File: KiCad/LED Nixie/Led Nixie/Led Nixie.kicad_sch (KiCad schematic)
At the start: 26 parts, among them J1 Conn_01x06_Socket, J2 Conn_01x06_Socket, J3 Conn_01x06_Pin, J4 Conn_01x06_Pin, U1 74HC595, U2 74HC595

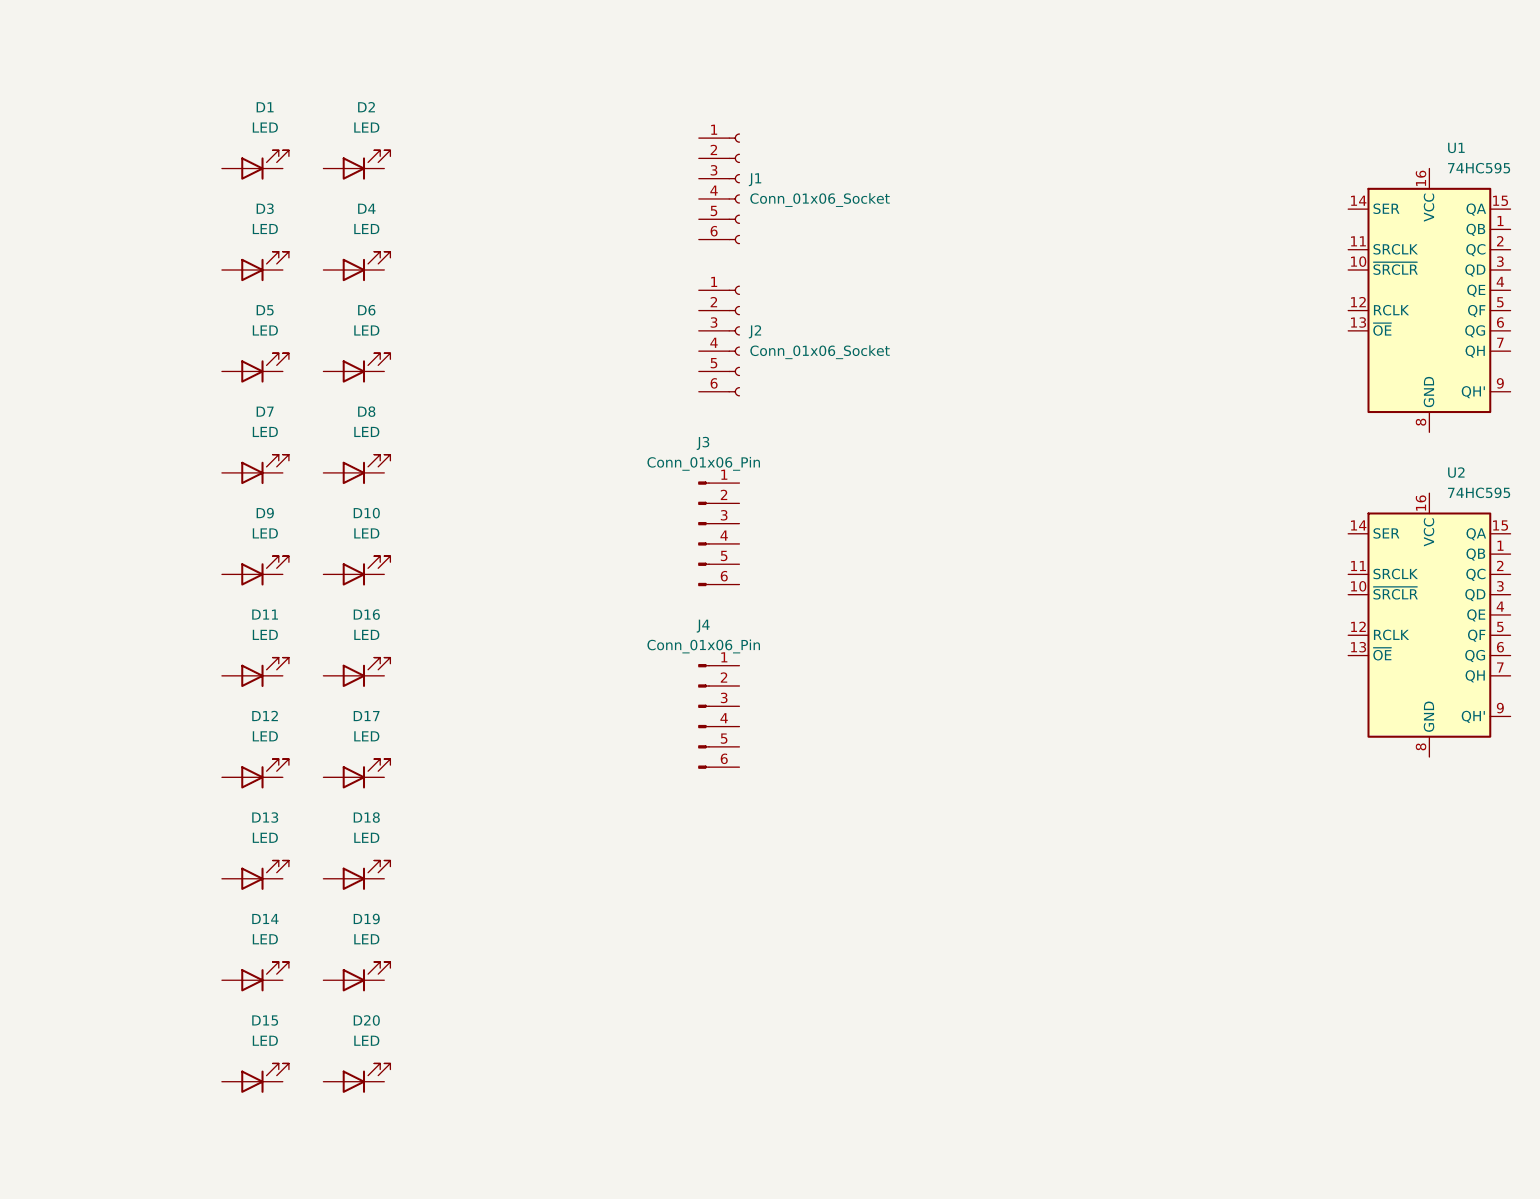
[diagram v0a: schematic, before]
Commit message: Updated Nixie-PCB
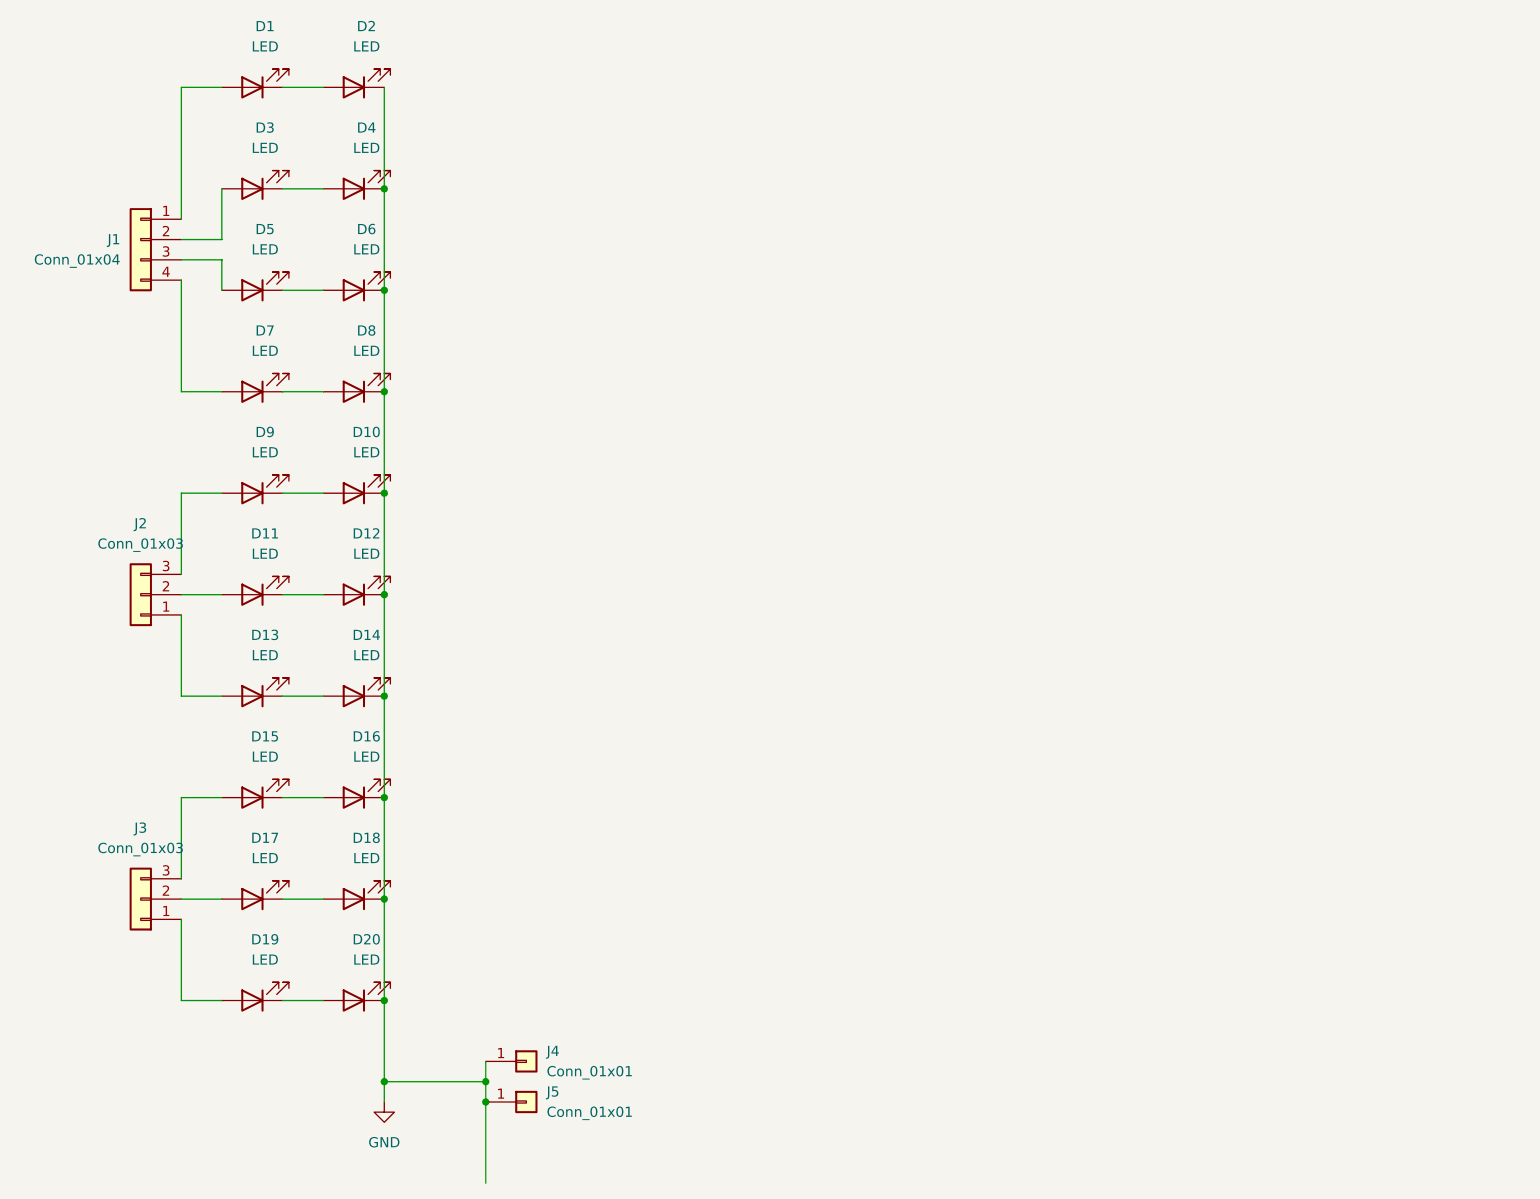
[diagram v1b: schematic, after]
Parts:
- removed J1, J2: Conn_01x06_Socket, symbol Connector:Conn_01x06_Socket
- removed J3, J4: Conn_01x06_Pin, symbol Connector:Conn_01x06_Pin
- removed U1, U2: 74HC595, symbol 74xx:74HC595
- added J1: Conn_01x04, Connector_PinHeader_2.00mm:PinHeader_1x04_P2.00mm_Vertical, symbol Connector_Generic:Conn_01x04
- added J2, J3: Conn_01x03, Connector_PinHeader_2.00mm:PinHeader_1x03_P2.00mm_Vertical, symbol Connector_Generic:Conn_01x03
- added J4, J5: Conn_01x01, Connector_PinHeader_2.00mm:PinHeader_1x01_P2.00mm_Vertical, symbol Connector_Generic:Conn_01x01
- D1, D10, D11, D2, D20, D3, D4, D5, D6, D7, D8, D9: footprint LED_SMD:LED_1206_3216Metric -> custom_footprints:LED_1206_3216Metric_nosilkscreen
- D12: renamed from D16; footprint LED_SMD:LED_1206_3216Metric -> custom_footprints:LED_1206_3216Metric_nosilkscreen
- D13: renamed from D12; footprint LED_SMD:LED_1206_3216Metric -> custom_footprints:LED_1206_3216Metric_nosilkscreen
- D14: renamed from D17; footprint LED_SMD:LED_1206_3216Metric -> custom_footprints:LED_1206_3216Metric_nosilkscreen
- D15: renamed from D13; footprint LED_SMD:LED_1206_3216Metric -> custom_footprints:LED_1206_3216Metric_nosilkscreen
- D16: renamed from D18; footprint LED_SMD:LED_1206_3216Metric -> custom_footprints:LED_1206_3216Metric_nosilkscreen
- D17: renamed from D14; footprint LED_SMD:LED_1206_3216Metric -> custom_footprints:LED_1206_3216Metric_nosilkscreen
- D18: renamed from D19; footprint LED_SMD:LED_1206_3216Metric -> custom_footprints:LED_1206_3216Metric_nosilkscreen
- D19: renamed from D15; footprint LED_SMD:LED_1206_3216Metric -> custom_footprints:LED_1206_3216Metric_nosilkscreen
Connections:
- net GND: now reaches D14.1 (K)
- net GND: now also D10.1 (K), D12.1 (K), D16.1 (K), D18.1 (K), D2.1 (K), D20.1 (K), D4.1 (K), D6.1 (K), D8.1 (K), J4.1 (Pin_1), J5.1 (Pin_1)
- net at D14.2 (A): now also D13.1 (K)
- net at D17.1 (K): now also D18.2 (A)
- net at D17.2 (A): now also J3.2 (Pin_2)
- net at D2.2 (A): now also D1.1 (K)
- net at D15.1 (K): now also D16.2 (A)
- net at D15.2 (A): now also J3.3 (Pin_3)
- net at D12.2 (A): now also D11.1 (K)
- net at D9.1 (K): now also D10.2 (A)
- net at D9.2 (A): now also J2.3 (Pin_3)
- net at D5.1 (K): now also D6.2 (A)
- net at D5.2 (A): now also J1.3 (Pin_3)
- net at D11.2 (A): now also J2.2 (Pin_2)
- net at D7.1 (K): now also D8.2 (A)
- net at D7.2 (A): now also J1.4 (Pin_4)
- net at D20.2 (A): now also D19.1 (K)
- net at D13.2 (A): now also J2.1 (Pin_1)
- net at D3.1 (K): now also D4.2 (A)
- net at D3.2 (A): now also J1.2 (Pin_2)
- net at D1.2 (A): now also J1.1 (Pin_1)
- net at D19.2 (A): now also J3.1 (Pin_1)
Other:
- moved on the sheet: D1, D10, D11, D12, D13, D14, D15, D16, D17, D18, D19, D2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

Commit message: updated PCB
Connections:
- net at D15.2 (A): now also J3.1 (Pin_1); no longer J3.3 (Pin_3)
- net at J2.1 (Pin_1): now also D9.2 (A); no longer D13.2 (A)
- net at J2.3 (Pin_3): now also D13.2 (A); no longer D9.2 (A)
- net at D19.2 (A): now also J3.3 (Pin_3); no longer J3.1 (Pin_1)
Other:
- moved on the sheet: J2, J3
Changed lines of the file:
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@@
 	(symbol
 		(lib_id "Connector_Generic:Conn_01x03")
-		(at 58.42 101.6 180)
-		(unit 1)
-		(exclude_from_sim no)
-		(in_bom yes)
-		(on_board yes)
-		(dnp no)
-		(fields_autoplaced yes)
+		(at 58.42 101.6 0)
+		(mirror y)
+		(unit 1)
+		(exclude_from_sim no)
+		(in_bom yes)
+		(on_board yes)
+		(dnp no)
 		(property "Reference" "J2"
-			(at 58.42 92.71 0)
+			(at 58.42 110.49 0)
 			(effects
 				(font
@@
 		)
 		(property "Value" "Conn_01x03"
-			(at 58.42 95.25 0)
+			(at 58.42 107.95 0)
 			(effects
 				(font
@@
 	(symbol
 		(lib_id "Connector_Generic:Conn_01x03")
-		(at 58.42 139.7 180)
-		(unit 1)
-		(exclude_from_sim no)
-		(in_bom yes)
-		(on_board yes)
-		(dnp no)
-		(fields_autoplaced yes)
+		(at 58.42 139.7 0)
+		(mirror y)
+		(unit 1)
+		(exclude_from_sim no)
+		(in_bom yes)
+		(on_board yes)
+		(dnp no)
 		(property "Reference" "J3"
-			(at 58.42 130.81 0)
+			(at 58.42 148.59 0)
 			(effects
 				(font
@@
 		)
 		(property "Value" "Conn_01x03"
-			(at 58.42 133.35 0)
-			(effects
-				(font
+			(at 58.42 146.05 0)
+			(effects
+				(font
